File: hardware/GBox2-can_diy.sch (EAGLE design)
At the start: 20 parts, among them IC1 PIC18F26K80, IC2 ISO1050

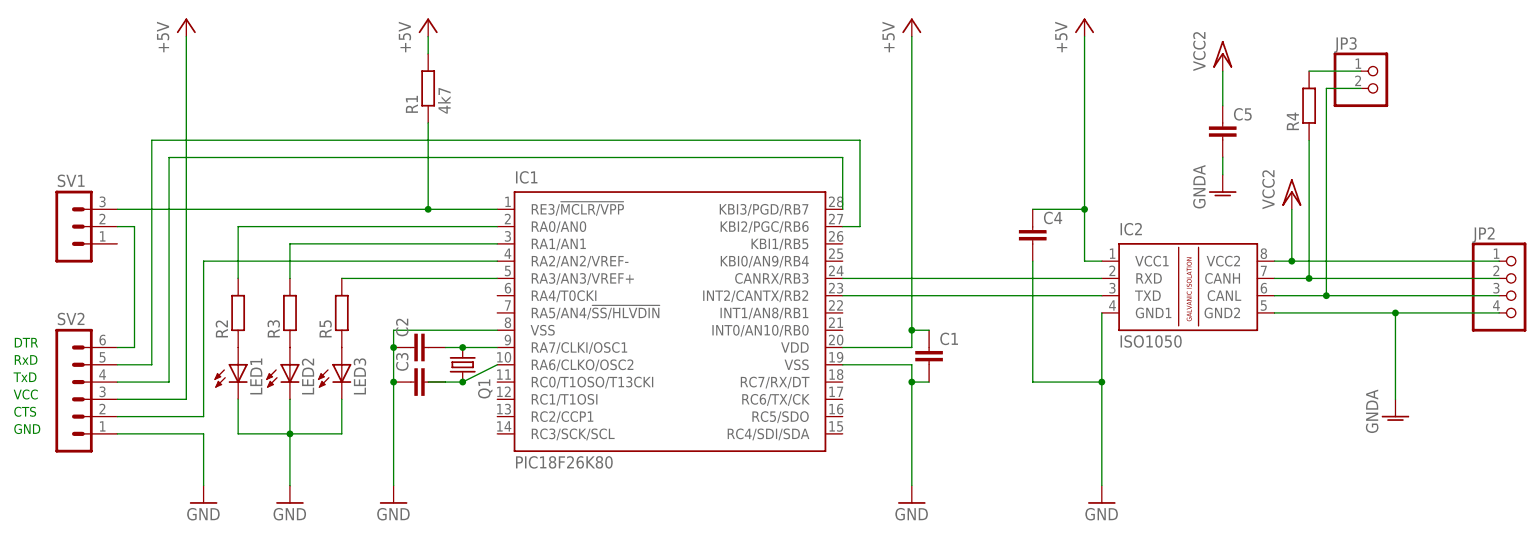
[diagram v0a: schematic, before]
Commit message: update schematic
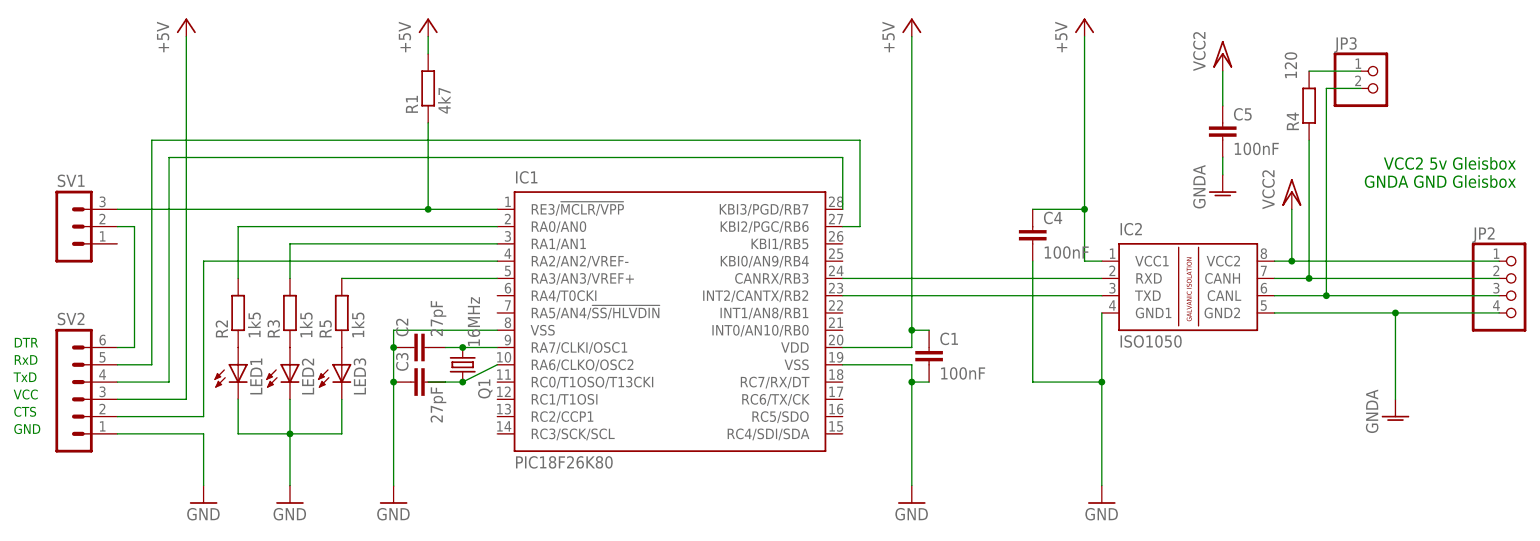
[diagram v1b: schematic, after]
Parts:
- C1, C4, C5: value (none) -> 100nF
- C2, C3: value (none) -> 27pF
- Q1: value (none) -> 16MHz
- R2, R3, R5: value (none) -> 1k5
- R4: value (none) -> 120
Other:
- note added: "VCC2 5v Gleisbox GNDA GND Gleisbox"
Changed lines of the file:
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@@
 <?xml version="1.0" encoding="utf-8"?>
 <!DOCTYPE eagle SYSTEM "eagle.dtd">
-<eagle version="6.5.0">
+<eagle version="6.6.0">
 <drawing>
 <settings>
@@
 <part name="R1" library="resistor" deviceset="R-EU_" device="R1206" value="4k7"/>
 <part name="P+3" library="supply1" deviceset="+5V" device=""/>
-<part name="C1" library="resistor" deviceset="C-EU" device="C1206"/>
-<part name="Q1" library="crystal" deviceset="CRYSTAL" device="HC49UP"/>
-<part name="C2" library="resistor" deviceset="C-EU" device="C1206"/>
-<part name="C3" library="resistor" deviceset="C-EU" device="C1206"/>
+<part name="C1" library="resistor" deviceset="C-EU" device="C1206" value="100nF"/>
+<part name="Q1" library="crystal" deviceset="CRYSTAL" device="HC49UP" value="16MHz"/>
+<part name="C2" library="resistor" deviceset="C-EU" device="C1206" value="27pF"/>
+<part name="C3" library="resistor" deviceset="C-EU" device="C1206" value="27pF"/>
 <part name="GND4" library="supply1" deviceset="GND" device=""/>
-<part name="R2" library="resistor" deviceset="R-EU_" device="R1206"/>
+<part name="R2" library="resistor" deviceset="R-EU_" device="R1206" value="1k5"/>
 <part name="IC2" library="texas" deviceset="ISO1050" device="DUB" value="ISO1050"/>
 <part name="GND5" library="supply1" deviceset="GND" device=""/>
 <part name="P+4" library="supply1" deviceset="+5V" device=""/>
-<part name="R4" library="resistor" deviceset="R-EU_" device="0204/7"/>
+<part name="R4" library="resistor" deviceset="R-EU_" device="0204/7" value="120"/>
 <part name="JP2" library="pinhead" deviceset="PINHD-1X4" device=""/>
 <part name="JP3" library="pinhead" deviceset="PINHD-1X2" device=""/>
-<part name="C4" library="resistor" deviceset="C-EU" device="C1206"/>
+<part name="C4" library="resistor" deviceset="C-EU" device="C1206" value="100nF"/>
 <part name="P+6" library="supply1" deviceset="VCC/2" device="" value="VCC2"/>
 <part name="GND7" library="supply1" deviceset="GNDA" device=""/>
-<part name="C5" library="resistor" deviceset="C-EU" device="C1206"/>
+<part name="C5" library="resistor" deviceset="C-EU" device="C1206" value="100nF"/>
 <part name="P+7" library="supply1" deviceset="VCC/2" device="" value="VCC2"/>
 <part name="GND8" library="supply1" deviceset="GNDA" device=""/>
@@
 <part name="SV2" library="con-lstb" deviceset="MA06-1" device=""/>
 <part name="LED2" library="led" deviceset="LED" device="SML1206"/>
-<part name="R3" library="resistor" deviceset="R-EU_" device="R1206"/>
-<part name="R5" library="resistor" deviceset="R-EU_" device="R1206"/>
+<part name="R3" library="resistor" deviceset="R-EU_" device="R1206" value="1k5"/>
+<part name="R5" library="resistor" deviceset="R-EU_" device="R1206" value="1k5"/>
 <part name="LED3" library="led" deviceset="LED" device="SML1206"/>
 </parts>
@@
 <text x="68.58" y="48.26" size="1.4224" layer="91">RxD</text>
 <text x="68.58" y="40.64" size="1.4224" layer="91">CTS</text>
+<text x="289.56" y="78.74" size="1.778" layer="91" rot="R180">VCC2 5v Gleisbox
+GNDA GND Gleisbox</text>
 </plain>
 <instances>
@@
 </instance>
 <instance part="C2" gate="G$1" x="127" y="50.8" rot="R90"/>
-<instance part="C3" gate="G$1" x="127" y="45.72" rot="R90"/>
+<instance part="C3" gate="G$1" x="127" y="45.72" smashed="yes" rot="R90">
+<attribute name="NAME" x="126.619" y="47.244" size="1.778" layer="95" rot="R90"/>
+<attribute name="VALUE" x="131.699" y="39.624" size="1.778" layer="96" rot="R90"/>
+</instance>
 <instance part="GND4" gate="1" x="124.46" y="27.94"/>
 <instance part="R2" gate="G$1" x="101.6" y="55.88" rot="R90"/>
@@
 <instance part="GND5" gate="1" x="228.6" y="27.94"/>
 <instance part="P+4" gate="1" x="226.06" y="99.06"/>
-<instance part="R4" gate="G$1" x="259.08" y="86.36" rot="R90"/>
+<instance part="R4" gate="G$1" x="259.08" y="86.36" smashed="yes" rot="R90">
+<attribute name="NAME" x="257.5814" y="82.55" size="1.778" layer="95" rot="R90"/>
+<attribute name="VALUE" x="257.302" y="90.17" size="1.778" layer="96" rot="R90"/>
+</instance>
 <instance part="JP2" gate="A" x="289.56" y="58.42"/>
 <instance part="JP3" gate="G$1" x="269.24" y="88.9"/>
@@
 </schematic>
 </drawing>
+<compatibility>
+<note version="6.3" minversion="6.2.2" severity="warning">
+Since Version 6.2.2 text objects can contain more than one line,
+which will not be processed correctly with this version.
+</note>
+</compatibility>
 </eagle>
